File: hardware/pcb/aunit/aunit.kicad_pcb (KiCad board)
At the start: 2 copper layers, 62.2 x 21.6 mm, 47 parts, among them J1 BUS, J2 Input A, J3 Input B, J4 Control, J5 Flags, J6 Power, U1 74HC283, U2 74HC283, U3 74HC86, U4 74HC86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

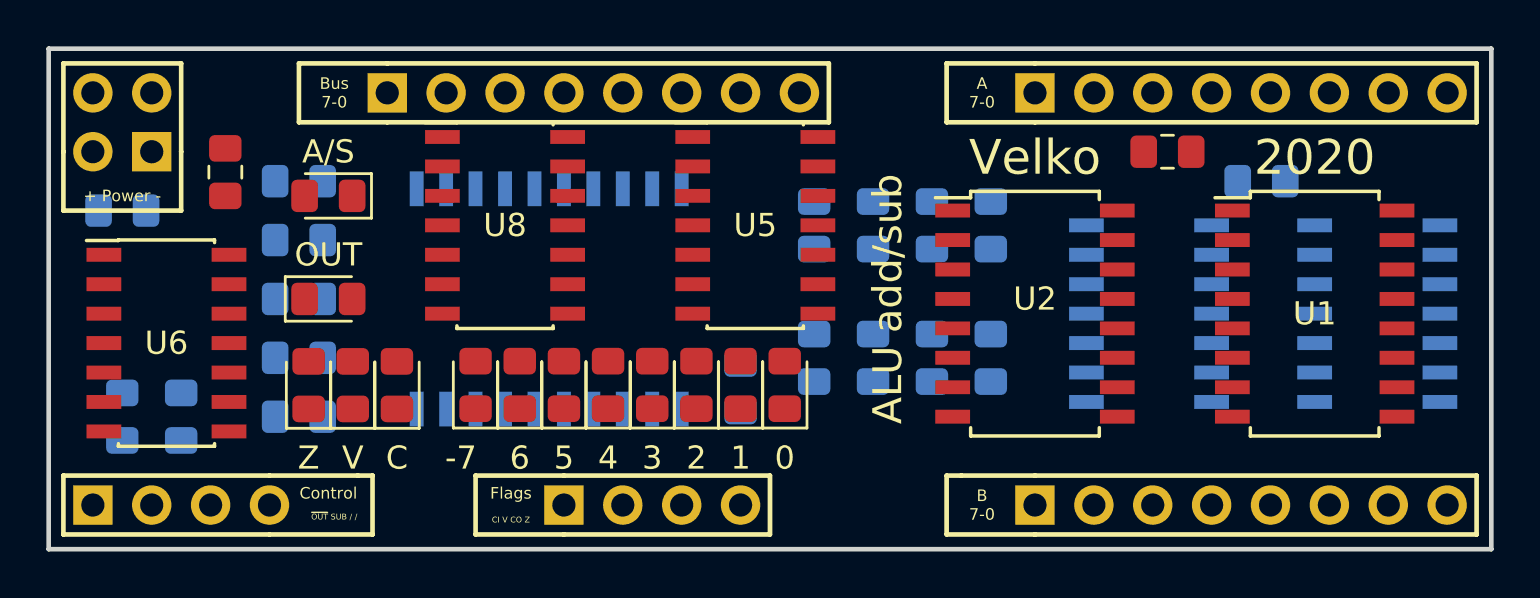
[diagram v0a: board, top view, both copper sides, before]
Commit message: Shuffle things around until board becomes routable
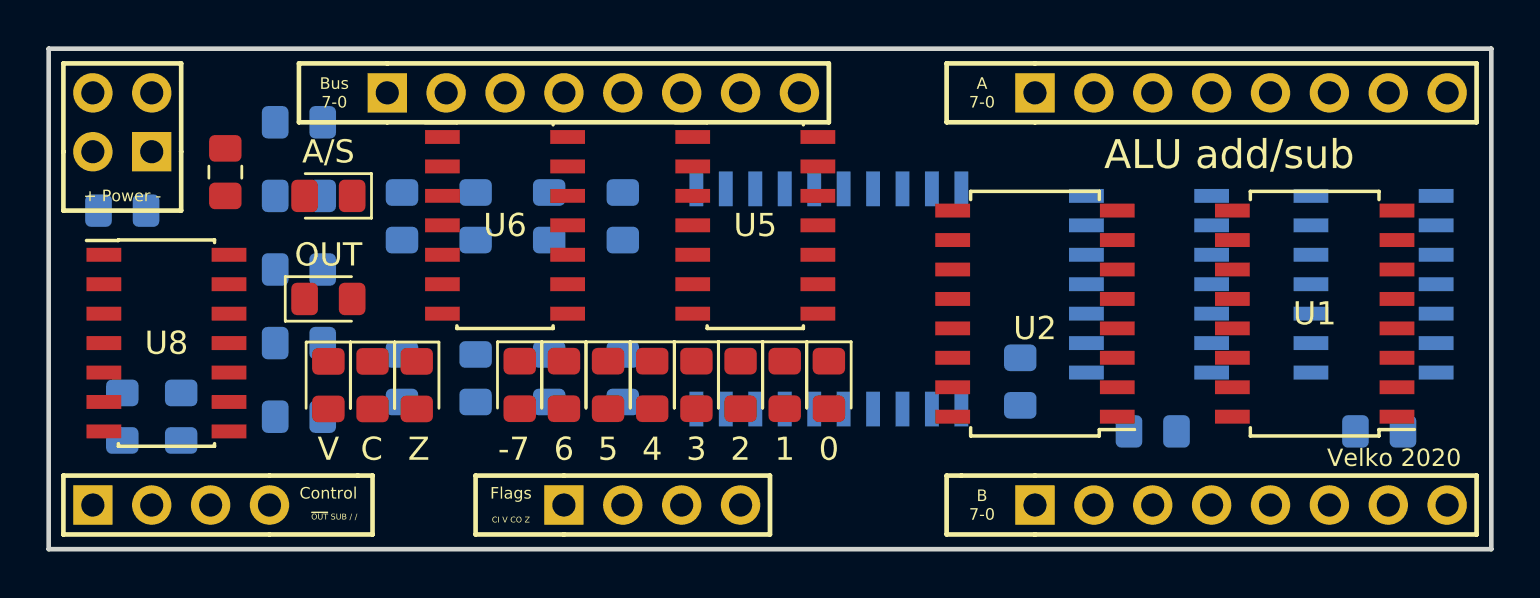
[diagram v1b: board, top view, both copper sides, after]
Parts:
- C4: moved to B.Cu
- moved R0 26.2 mm to (50.2, 50.4), turned to 90 degrees
- moved R1 20.8 mm to (53.3, 50.4), turned to 90 degrees
- moved R7 17.8 mm to (50.2, 43.4)
- moved R3 15.9 mm to (59.7, 50.4), turned to 90 degrees
- moved R6 15.8 mm to (53.3, 43.4)
- moved U6 15.5 mm to (54.6, 43.8)
- moved U8 15.5 mm to (40.0, 48.9)
- moved R2 15.4 mm to (56.5, 50.4), turned to 90 degrees
- moved R5 15.2 mm to (56.5, 43.4)
- moved R4 14.7 mm to (59.7, 43.4)
- moved C4 12.1 mm to (82.5, 52.7), turned to 180 degrees
- moved C2 12.1 mm to (76.8, 50.6)
- moved U7 12.1 mm to (68.6, 47.0)
- moved C5 11.9 mm to (92.3, 52.7), turned to 180 degrees
- moved D12 4.66 mm to (50.8, 50.7), turned to 270 degrees
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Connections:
- net Net-(U2-Pad9) renamed /CO
- U1 pad 11: Net-(U1-Pad11) -> /B3I
- U1 pad 15: Net-(U1-Pad15) -> /B2I
- U1 pad 2: Net-(U1-Pad2) -> /B1I
- U1 pad 6: Net-(U1-Pad6) -> /B0I
- U1 pad 7: Net-(U1-Pad7) -> /CII
- U2 pad 15: Net-(U2-Pad15) -> /B6I
- U2 pad 2: Net-(U2-Pad2) -> /B5I
- U2 pad 6: Net-(U2-Pad6) -> /B4I
- U3 pad 1: B0 -> B2
- U3 pad 10: ADD_SUB -> B0
- U3 pad 11: Net-(U1-Pad11) -> /B1I
- U3 pad 12: B3 -> ADD_SUB
- U3 pad 13: ADD_SUB -> B1
- U3 pad 3: Net-(U1-Pad6) -> /B2I
- U3 pad 4: B1 -> B3
- U3 pad 6: Net-(U1-Pad2) -> /B3I
- U3 pad 8: Net-(U1-Pad15) -> /B0I
- U3 pad 9: B2 -> ADD_SUB
- U4 pad 1: B4 -> B7
- U4 pad 10: ADD_SUB -> B4
- U4 pad 11: B7I -> /B5I
- U4 pad 12: B7 -> ADD_SUB
- U4 pad 13: ADD_SUB -> B5
- U4 pad 3: Net-(U2-Pad6) -> B7I
- U4 pad 4: B5 -> B6
- U4 pad 6: Net-(U2-Pad2) -> /B6I
- U4 pad 8: Net-(U2-Pad15) -> /B4I
- U4 pad 9: B6 -> ADD_SUB
- U5 pad 1: CIN -> A7
- U5 pad 10: B7I -> ADD_SUB
- U5 pad 13: A0 -> A7
- U5 pad 2: ADD_SUB -> B7I
- U5 pad 3: Net-(U1-Pad7) -> Net-(U5-Pad3)
- U5 pad 8: Net-(U5-Pad8) -> /CII
- U5 pad 9: A0 -> CIN
- U6 pad 1: Net-(U5-Pad8) -> VCC
- U6 pad 11: Net-(U6-Pad11) -> Net-(U6-Pad10)
- U6 pad 12: VCC -> Net-(U5-Pad3)
- U6 pad 13: VCC -> Net-(U5-Pad3)
- U6 pad 2: Net-(U5-Pad8) -> VCC
- U6 pad 4: Net-(U6-Pad3) -> Net-(U6-Pad4)
- U6 pad 5: Net-(U5-Pad11) -> Net-(U6-Pad4)
- U6 pad 6: Net-(U6-Pad10) -> OVFD
- U6 pad 8: OVFD -> Net-(U6-Pad4)
- U6 pad 9: Net-(U6-Pad10) -> Net-(U5-Pad11)
- U7 pad 11: BUS0 -> BUS7
- U7 pad 12: BUS1 -> BUS6
- U7 pad 13: BUS2 -> BUS5
- U7 pad 14: BUS3 -> BUS4
- U7 pad 15: BUS4 -> BUS3
- U7 pad 16: BUS5 -> BUS2
- U7 pad 17: BUS6 -> BUS1
- U7 pad 18: BUS7 -> BUS0
- U7 pad 2: SUM7 -> SUM0
- U7 pad 3: SUM6 -> SUM1
- U7 pad 4: SUM5 -> SUM2
- U7 pad 5: SUM4 -> SUM3
- U7 pad 6: SUM3 -> SUM4
- U7 pad 7: SUM2 -> SUM5
- U7 pad 8: SUM1 -> SUM6
- U7 pad 9: SUM0 -> SUM7
- U8 pad 2: OVFD -> CARRYD
- U8 pad 3: OOUT -> COUT
- U8 pad 5: CARRYD -> OVFD
- U8 pad 6: COUT -> OOUT
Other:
- board text added: "Velko 2020"
- board text removed: "2020"
- board text removed: "Velko"

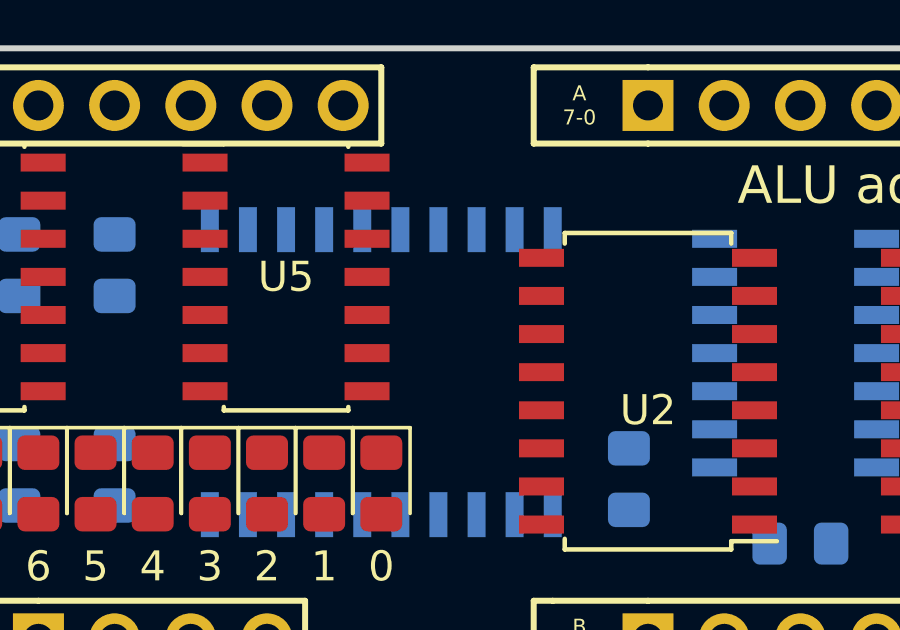
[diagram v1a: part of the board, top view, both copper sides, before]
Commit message: Add SBB/SBC jumper
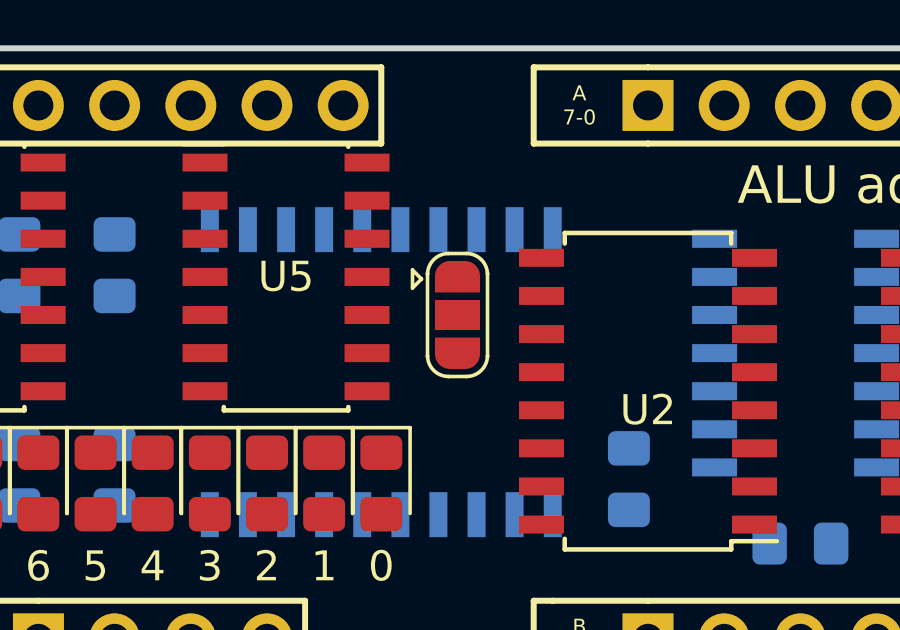
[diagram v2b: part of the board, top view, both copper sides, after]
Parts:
- added JP1: SolderJumper_3_Open, Jumper:SolderJumper-3_P1.3mm_Open_RoundedPad1.0x1.5mm, F.Cu at (71.1, 45.1)
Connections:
- U5 pad 10: ADD_SUB -> Net-(JP1-Pad2)
- U5 pad 5: ADD_SUB -> Net-(JP1-Pad2)
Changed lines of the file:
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@@
     (tracks 0)
     (zones 0)
-    (modules 47)
-    (nets 76)
+    (modules 48)
+    (nets 77)
   )
   (page A4)
   (layers
-    (0 F.Cu signal hide)
-    (31 B.Cu signal)
+    (0 F.Cu signal)
+    (31 B.Cu signal hide)
     (32 B.Adhes user hide)
     (33 F.Adhes user hide)
@@
     (35 F.Paste user hide)
     (36 B.SilkS user)
-    (37 F.SilkS user hide)
+    (37 F.SilkS user)
     (38 B.Mask user hide)
     (39 F.Mask user hide)
@@
   (net 74 "Net-(U5-Pad3)")
   (net 75 "Net-(U6-Pad4)")
+  (net 76 "Net-(JP1-Pad2)")
   (net_class Default "This is the default net class."
     (clearance 0.2)
@@
     (add_net "Net-(J4-Pad3)")
     (add_net "Net-(J4-Pad4)")
+    (add_net "Net-(JP1-Pad2)")
     (add_net "Net-(U1-Pad9)")
     (add_net "Net-(U5-Pad11)")
@@
       (net 72 /CO))
     (pad 5 smd rect (at -2.7 1.27) (size 1.5 0.6) (layers F.Cu F.Paste F.Mask)
-      (net 26 ADD_SUB))
+      (net 76 "Net-(JP1-Pad2)"))
     (pad 6 smd rect (at -2.7 2.54) (size 1.5 0.6) (layers F.Cu F.Paste F.Mask)
       (net 23 CARRYD))
@@
       (net 58 CIN))
     (pad 10 smd rect (at 2.7 1.27) (size 1.5 0.6) (layers F.Cu F.Paste F.Mask)
-      (net 26 ADD_SUB))
+      (net 76 "Net-(JP1-Pad2)"))
     (pad 11 smd rect (at 2.7 0) (size 1.5 0.6) (layers F.Cu F.Paste F.Mask)
       (net 61 "Net-(U5-Pad11)"))
@@
     )
   )
+  (module Jumper:SolderJumper-3_P1.3mm_Open_RoundedPad1.0x1.5mm (layer F.Cu)
+    (at 71.12 45.085 270)
+    (descr "SMD Solder 3-pad Jumper, 1x1.5mm rounded Pads, 0.3mm gap, open")
+    (tags "solder jumper open")
+    (attr virtual)
+    (fp_text reference JP1 (at 0 -1.8 270) (layer F.SilkS) hide
+      (effects (font (size 1 1) (thickness 0.15)))
+    )
+    (fp_text value SolderJumper_3_Open (at 0 1.9 270) (layer F.Fab)
+      (effects (font (size 1 1) (thickness 0.15)))
+    )
+    (fp_line (start -1.2 1.2) (end -0.9 1.5) (layer F.SilkS) (width 0.12))
+    (fp_line (start -1.5 1.5) (end -0.9 1.5) (layer F.SilkS) (width 0.12))
+    (fp_line (start -1.2 1.2) (end -1.5 1.5) (layer F.SilkS) (width 0.12))
+    (fp_line (start -2.05 0.3) (end -2.05 -0.3) (layer F.SilkS) (width 0.12))
+    (fp_line (start 1.4 1) (end -1.4 1) (layer F.SilkS) (width 0.12))
+    (fp_line (start 2.05 -0.3) (end 2.05 0.3) (layer F.SilkS) (width 0.12))
+    (fp_line (start -1.4 -1) (end 1.4 -1) (layer F.SilkS) (width 0.12))
+    (fp_line (start -2.3 -1.25) (end 2.3 -1.25) (layer F.CrtYd) (width 0.05))
+    (fp_line (start -2.3 -1.25) (end -2.3 1.25) (layer F.CrtYd) (width 0.05))
+    (fp_line (start 2.3 1.25) (end 2.3 -1.25) (layer F.CrtYd) (width 0.05))
+    (fp_line (start 2.3 1.25) (end -2.3 1.25) (layer F.CrtYd) (width 0.05))
+    (fp_arc (start 1.35 -0.3) (end 2.05 -0.3) (angle -90) (layer F.SilkS) (width 0.12))
+    (fp_arc (start 1.35 0.3) (end 1.35 1) (angle -90) (layer F.SilkS) (width 0.12))
+    (fp_arc (start -1.35 0.3) (end -2.05 0.3) (angle -90) (layer F.SilkS) (width 0.12))
+    (fp_arc (start -1.35 -0.3) (end -1.35 -1) (angle -90) (layer F.SilkS) (width 0.12))
+    (pad 1 smd custom (at -1.3 0 270) (size 1 0.5) (layers F.Cu F.Mask)
+      (net 26 ADD_SUB) (zone_connect 0)
+      (options (clearance outline) (anchor rect))
+      (primitives
+        (gr_circle (center 0 0.25) (end 0.5 0.25) (width 0))
+        (gr_circle (center 0 -0.25) (end 0.5 -0.25) (width 0))
+        (gr_poly (pts
+           (xy 0.55 -0.75) (xy 0 -0.75) (xy 0 0.75) (xy 0.55 0.75)) (width 0))
+      ))
+    (pad 3 smd custom (at 1.3 0 270) (size 1 0.5) (layers F.Cu F.Mask)
+      (net 2 GND) (zone_connect 0)
+      (options (clearance outline) (anchor rect))
+      (primitives
+        (gr_circle (center 0 0.25) (end 0.5 0.25) (width 0))
+        (gr_circle (center 0 -0.25) (end 0.5 -0.25) (width 0))
+        (gr_poly (pts
+           (xy -0.55 -0.75) (xy 0 -0.75) (xy 0 0.75) (xy -0.55 0.75)) (width 0))
+      ))
+    (pad 2 smd rect (at 0 0 270) (size 1 1.5) (layers F.Cu F.Mask)
+      (net 76 "Net-(JP1-Pad2)"))
+  )
   (gr_line (start 40.64 36.83) (end 40.64 40.64) (layer F.SilkS) (width 0.2))

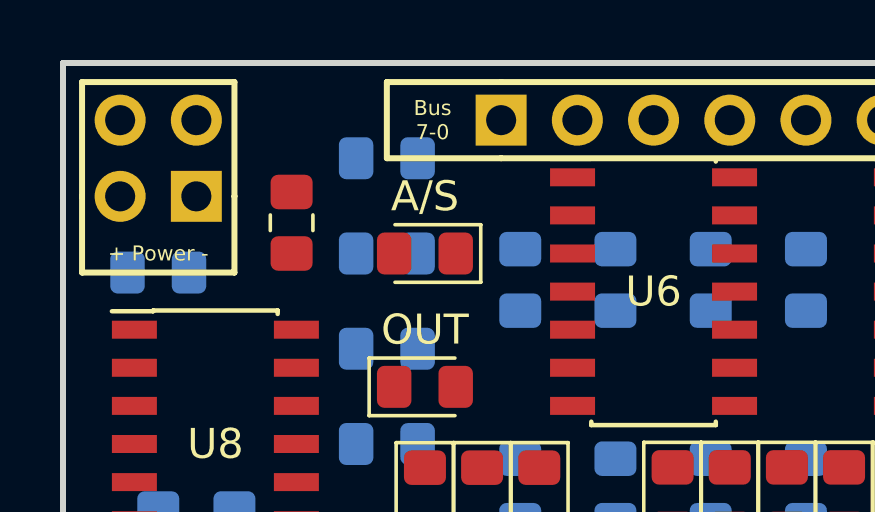
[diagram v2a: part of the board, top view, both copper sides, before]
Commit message: Rewire Overflow
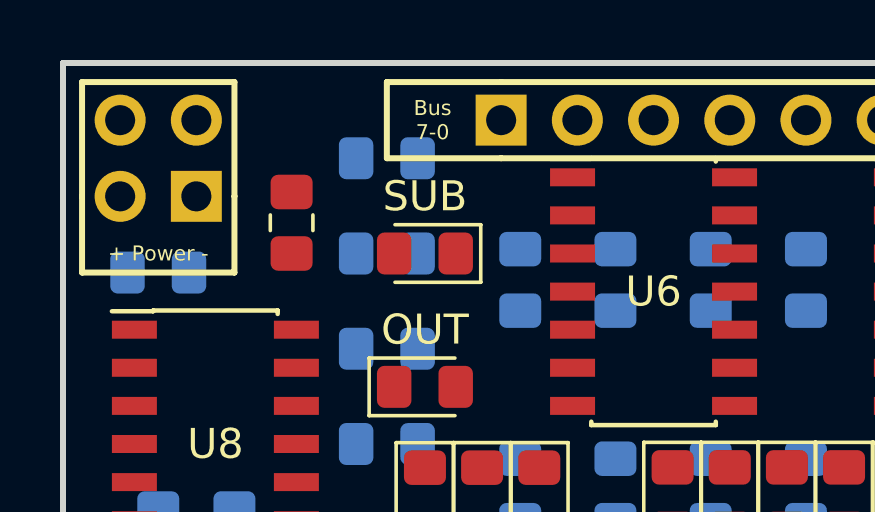
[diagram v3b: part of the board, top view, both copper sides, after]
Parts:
- D11: value A/S -> SUB
- U6: value 74HC00 -> 74HC08
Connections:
- D8 pad 1: Net-(D8-Pad1) -> ~OUT~
- D8 pad 2: ~OUT~ -> Net-(D8-Pad2)
- R8 pad 2: Net-(D8-Pad1) -> Net-(D8-Pad2)
- U5 pad 1: A7 -> B7I
- U5 pad 12: SUM7 -> A7
- U5 pad 13: A7 -> SUM7
- U5 pad 2: B7I -> SUM7
- U6 pad 10: Net-(U6-Pad10) -> Net-(U5-Pad3)
- U6 pad 11: Net-(U6-Pad10) -> Net-(U6-Pad11)
- U6 pad 12: Net-(U5-Pad3) -> VCC
- U6 pad 13: Net-(U5-Pad3) -> VCC
- U6 pad 4: Net-(U6-Pad4) -> VCC
- U6 pad 5: Net-(U6-Pad4) -> VCC
- U6 pad 6: OVFD -> Net-(U6-Pad6)
- U6 pad 8: Net-(U6-Pad4) -> OVFD

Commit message: Shuffle things around
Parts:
- turned D8 to 180 degrees
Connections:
- U6 pad 10: Net-(U5-Pad3) -> GND
- U6 pad 11: Net-(U6-Pad11) -> OVFD
- U6 pad 12: VCC -> Net-(U5-Pad11)
- U6 pad 13: VCC -> Net-(U5-Pad3)
- U6 pad 4: VCC -> GND
- U6 pad 5: VCC -> GND
- U6 pad 8: OVFD -> Net-(U6-Pad8)
- U6 pad 9: Net-(U5-Pad11) -> GND
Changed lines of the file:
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@@
   (layers
     (0 F.Cu signal)
-    (31 B.Cu signal)
+    (31 B.Cu signal hide)
     (32 B.Adhes user hide)
     (33 F.Adhes user hide)
@@
   (net 73 "Net-(JP1-Pad2)")
   (net 74 "Net-(D8-Pad2)")
-  (net 75 "Net-(U6-Pad11)")
-  (net 76 "Net-(U6-Pad6)")
+  (net 75 "Net-(U6-Pad6)")
+  (net 76 "Net-(U6-Pad8)")
   (net_class Default "This is the default net class."
     (clearance 0.2)
@@
     (add_net "Net-(U5-Pad11)")
     (add_net "Net-(U5-Pad3)")
-    (add_net "Net-(U6-Pad11)")
     (add_net "Net-(U6-Pad3)")
     (add_net "Net-(U6-Pad6)")
+    (add_net "Net-(U6-Pad8)")
     (add_net "Net-(U8-Pad11)")
     (add_net OOUT)
@@
   )
   (module LED_SMD:LED_0805_2012Metric_Pad1.15x1.40mm_HandSolder (layer F.Cu)
-    (at 46.99 46.99)
+    (at 46.99 46.99 180)
     (descr "LED SMD 0805 (2012 Metric), square (rectangular) end terminal, IPC_7351 nominal, (Body size source: https://docs.google.com/spreadsheets/d/1BsfQQcO9C6DZCsRaXUlFlo91Tg2WpOkGARC1WS5S8t0/edit?usp=sharing), generated with kicad-footprint-generator")
     (tags "LED handsolder")
@@
       (effects (font (size 1 1) (thickness 0.15)))
     )
-    (fp_text value OUT (at 0 -1.905) (layer F.SilkS)
+    (fp_text value OUT (at 0 1.778) (layer F.SilkS)
       (effects (font (size 1 1) (thickness 0.15)))
     )
@@
       (effects (font (size 0.5 0.5) (thickness 0.08)))
     )
-    (pad 1 smd roundrect (at -1.025 0) (size 1.15 1.4) (layers F.Cu F.Paste F.Mask) (roundrect_rratio 0.217391)
+    (pad 1 smd roundrect (at -1.025 0 180) (size 1.15 1.4) (layers F.Cu F.Paste F.Mask) (roundrect_rratio 0.217391)
       (net 19 ~OUT~))
-    (pad 2 smd roundrect (at 1.025 0) (size 1.15 1.4) (layers F.Cu F.Paste F.Mask) (roundrect_rratio 0.217391)
+    (pad 2 smd roundrect (at 1.025 0 180) (size 1.15 1.4) (layers F.Cu F.Paste F.Mask) (roundrect_rratio 0.217391)
       (net 74 "Net-(D8-Pad2)"))
     (model ${KISYS3DMOD}/LED_SMD.3dshapes/LED_0805_2012Metric.wrl
@@
       (net 1 VCC))
     (pad 13 smd rect (at 2.7 -2.54) (size 1.5 0.6) (layers F.Cu F.Paste F.Mask)
-      (net 1 VCC))
+      (net 72 "Net-(U5-Pad3)"))
     (pad 12 smd rect (at 2.7 -1.27) (size 1.5 0.6) (layers F.Cu F.Paste F.Mask)
-      (net 1 VCC))
+      (net 60 "Net-(U5-Pad11)"))
     (pad 11 smd rect (at 2.7 0) (size 1.5 0.6) (layers F.Cu F.Paste F.Mask)
-      (net 75 "Net-(U6-Pad11)"))
+      (net 20 OVFD))
     (pad 10 smd rect (at 2.7 1.27) (size 1.5 0.6) (layers F.Cu F.Paste F.Mask)
-      (net 72 "Net-(U5-Pad3)"))
+      (net 2 GND))
     (pad 9 smd rect (at 2.7 2.54) (size 1.5 0.6) (layers F.Cu F.Paste F.Mask)
-      (net 60 "Net-(U5-Pad11)"))
+      (net 2 GND))
     (pad 8 smd rect (at 2.7 3.81) (size 1.5 0.6) (layers F.Cu F.Paste F.Mask)
-      (net 20 OVFD))
+      (net 76 "Net-(U6-Pad8)"))
     (pad 7 smd rect (at -2.7 3.81) (size 1.5 0.6) (layers F.Cu F.Paste F.Mask)
       (net 2 GND))
     (pad 6 smd rect (at -2.7 2.54) (size 1.5 0.6) (layers F.Cu F.Paste F.Mask)
-      (net 76 "Net-(U6-Pad6)"))
+      (net 75 "Net-(U6-Pad6)"))
     (pad 5 smd rect (at -2.7 1.27) (size 1.5 0.6) (layers F.Cu F.Paste F.Mask)
-      (net 1 VCC))
+      (net 2 GND))
     (pad 4 smd rect (at -2.7 0) (size 1.5 0.6) (layers F.Cu F.Paste F.Mask)
-      (net 1 VCC))
+      (net 2 GND))
     (pad 3 smd rect (at -2.7 -1.27) (size 1.5 0.6) (layers F.Cu F.Paste F.Mask)
       (net 61 "Net-(U6-Pad3)"))

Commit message: Disconnect inputs of unused gates to ease routing
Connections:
- U6 pad 1: VCC -> Net-(U6-Pad1)
- U6 pad 10: GND -> Net-(U6-Pad10)
- U6 pad 2: VCC -> Net-(U6-Pad2)
- U6 pad 4: GND -> Net-(U6-Pad4)
- U6 pad 5: GND -> Net-(U6-Pad5)
- U6 pad 9: GND -> Net-(U6-Pad9)

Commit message: Imported autorouted
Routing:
- net GND: track 0.00 -> 209.5 mm, vias 0 -> 5
- net ADD_SUB: track 0.00 -> 137.9 mm, vias 0 -> 2
- net VCC: track 0.00 -> 124.4 mm, vias 0 -> 3
- net ~OUT~: track 0.00 -> 85.6 mm
- net CARRYD: track 0.00 -> 44.2 mm
- net SUM7: track 0.00 -> 41.3 mm, vias 0 -> 2
- net COUT: track 0.00 -> 37.9 mm
- net OVFD: track 0.00 -> 36.4 mm
- net /CII: track 0.00 -> 35.0 mm, vias 0 -> 2
- net SUM1: track 0.00 -> 33.3 mm, vias 0 -> 2
- net SUM3: track 0.00 -> 32.8 mm, vias 0 -> 2
- net SUM0: track 0.00 -> 31.3 mm, vias 0 -> 2
- net SUM2: track 0.00 -> 29.5 mm, vias 0 -> 2
- net ZIN: track 0.00 -> 28.0 mm
- net SUM5: track 0.00 -> 27.9 mm, vias 0 -> 1
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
